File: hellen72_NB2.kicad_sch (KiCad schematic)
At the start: 186 parts, among them J1 USB_B_Mini, J11 Conn_01x01, J13 Conn_01x01, J14 Conn_01x01, J15 Conn_01x01, J16 Conn_01x01, J17 Conn_01x01, J19 Conn_01x01, J2 Conn_01x05_Male, J20 Conn_01x01, J21 Conn_01x01, J22 Conn_01x01, J24 Conn_01x01, J25 AudioJack3_SwitchTR, J27 Conn_01x06, J3 MiniFit, J4 Conn_02x12_Odd_Even, J5 USB_B, M1 Module-input-0.1, M10 Module-power12-0.2, M11 Module-power5-0.2, M12 Module-wbo-0.3, M13 Module-can-0.1, M2 Module-ign8-0.1, M3 Module-mcu-0.6, M4 Module-sd-0.1, M5 Module-output-0.3, M6 Module-dinput4-0.1, M7 Module-stlink-0.1, M8 Module-can-0.1, M9 Module-knock-0.1, P1 Pad, P10 Pad, P11 Pad, P12 Pad, P13 Pad, P15 Pad, P16 Pad, P17 Pad, P18 Pad, P19 Pad, P2 8-5353015-1, P20 Pad, P21 Pad, P23 Pad, P3 Pad, P4 Pad, P48 Pad, P49 Pad, P5 Pad, P50 Pad, P51 Pad, P52 Pad, P53 Pad, P56 Pad, P6 Pad, P7 Pad, P8 Pad, P9 Pad, Q1 AUIPS2041LTR, Q2 AUIPS2041LTR, U1 LIS2DW12TR, U2 MPX4_MAP, U3 MCP6002-xSN, U4 LPS25HB, U5 L6205PD

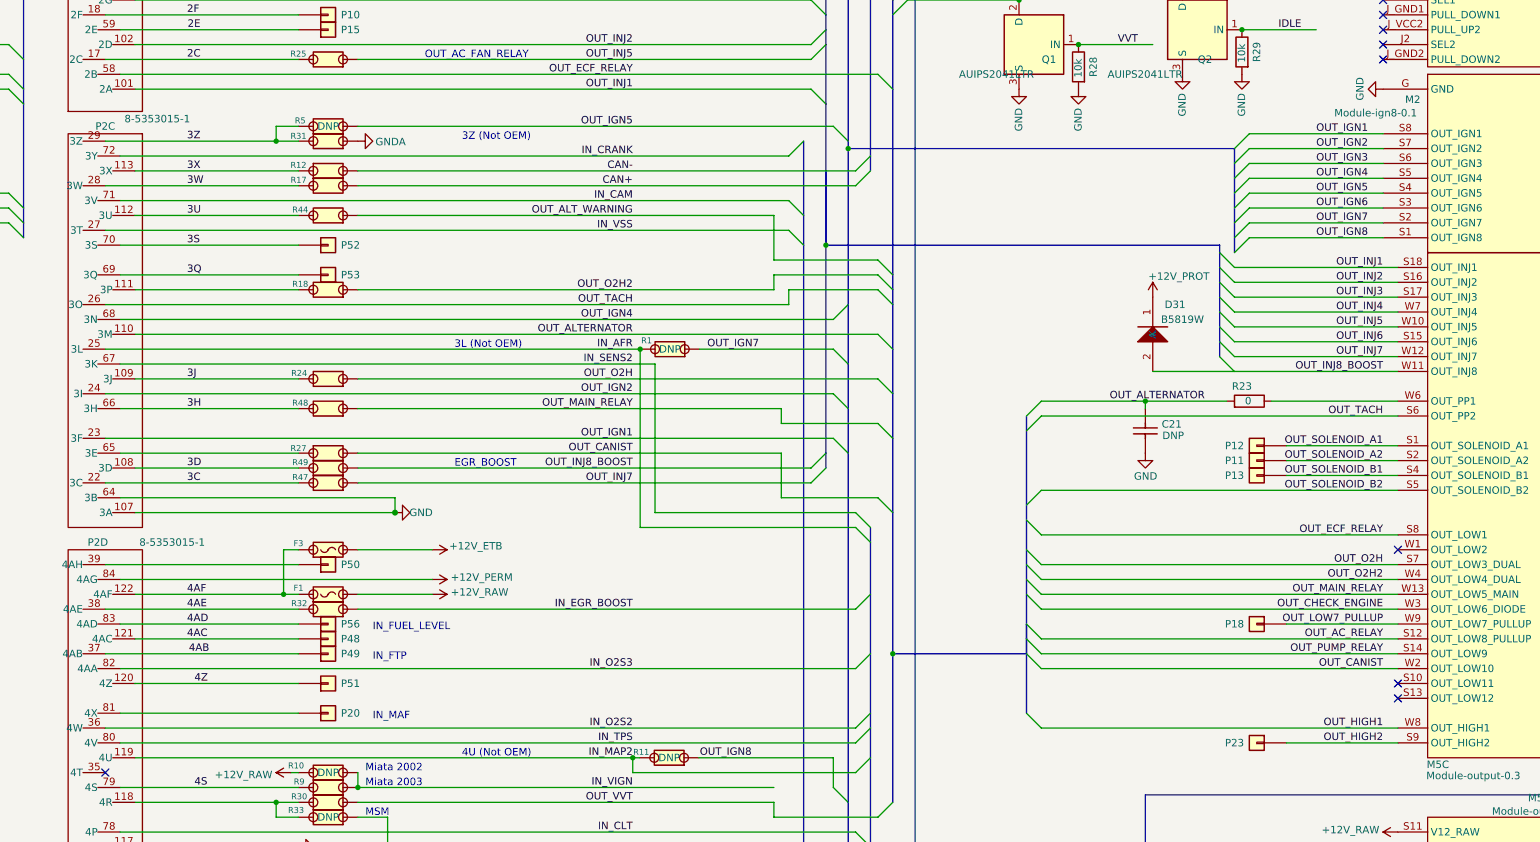
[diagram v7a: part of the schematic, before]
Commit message: https://github.com/rusefi/hellen-NB2-issues/issues/35
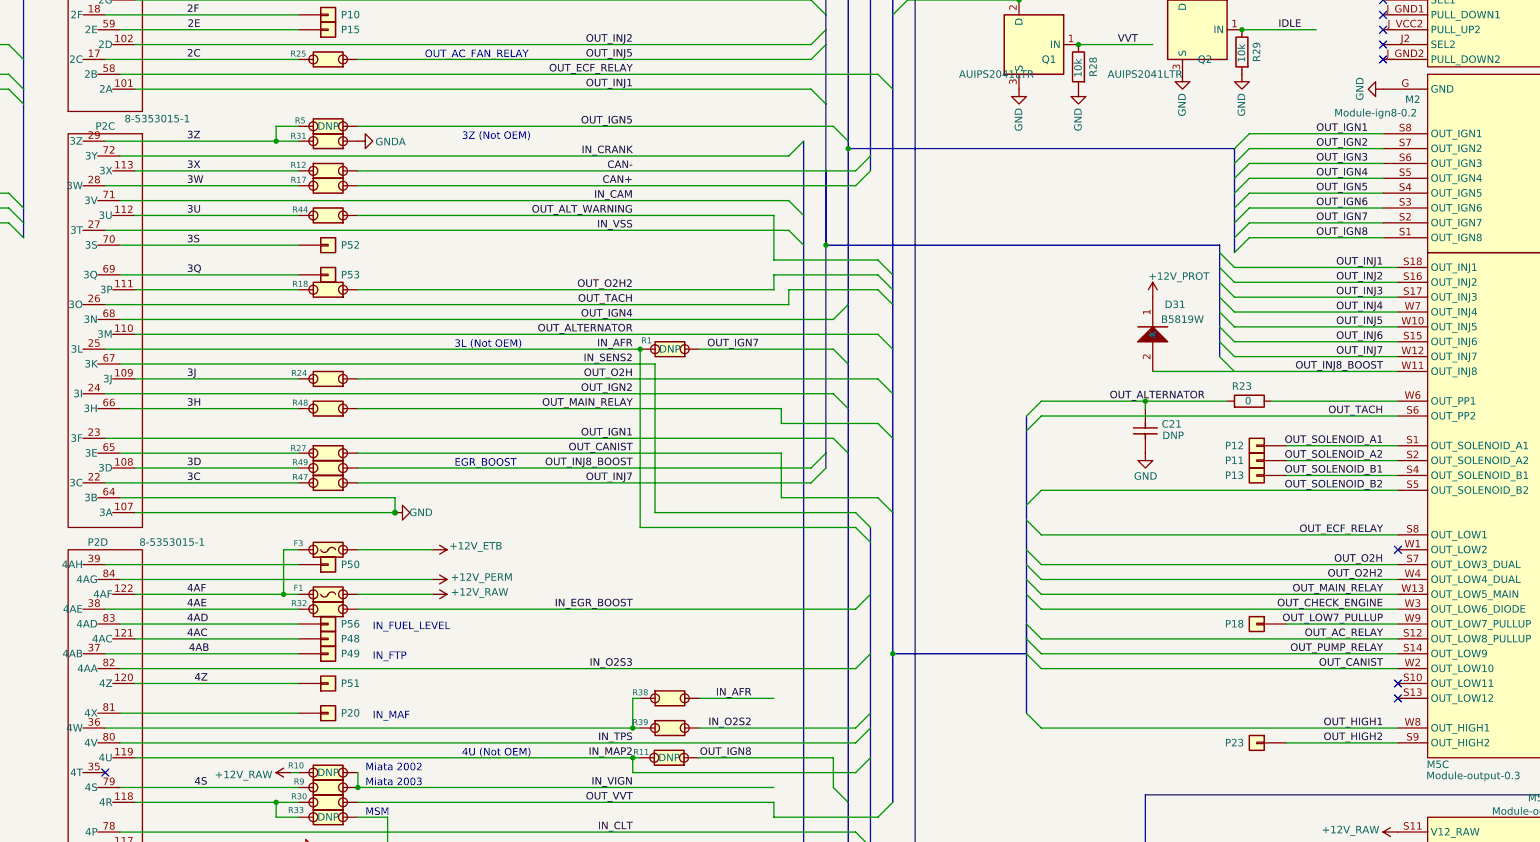
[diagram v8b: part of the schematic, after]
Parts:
- added R38, R39: Jumper-Pad-Pad, hellen-one-common:PAD-0805-PAD, symbol hellen-one-common:Jumper-Pad-Pad
- M2: value Module-ign8-0.1 -> Module-ign8-0.2; footprint hellen-one-ign8-0.1:ign8 -> hellen-one-ign8-0.2:ign8; symbol hellen-one-ign8-0.1:Module-ign8-0.1 -> hellen-one-ign8-0.2:Module-ign8-0.2
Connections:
- net IN_AFR: now also R38.2
- net IN_O2S2: now also R39.2; no longer P2.36 (4W)
- new net: P2.36 (4W), R38.1, R39.1
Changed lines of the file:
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@@
   (title_block
     (title "Hellen72 NB2")
-    (date "2022-03-28")
+    (date "2022-05-18")
     (rev "F")
     (company "rusEFI")
@@
   (junction (at 567.69 325.12) (diameter 1.016) (color 0 0 0 0)
   )
+  (junction (at 179.07 172.72) (diameter 0) (color 0 0 0 0)
+  )
   (junction (at 513.08 308.61) (diameter 1.016) (color 0 0 0 0)
   )
@@
     (stroke (width 0) (type solid) (color 0 0 0 0))
   )
+  (wire (pts (xy 179.07 172.72) (xy 180.34 172.72))
+    (stroke (width 0) (type solid) (color 0 0 0 0))
+  )
+  (wire (pts (xy 190.5 172.72) (xy 217.17 172.72))
+    (stroke (width 0) (type solid) (color 0 0 0 0))
+  )
   (wire (pts (xy 120.65 180.34) (xy 121.92 180.34))
     (stroke (width 0) (type default) (color 0 0 0 0))
@@
     (stroke (width 0) (type solid) (color 0 0 0 0))
   )
+  (wire (pts (xy 179.07 167.64) (xy 179.07 172.72))
+    (stroke (width 0) (type default) (color 0 0 0 0))
+  )
   (wire (pts (xy 88.9 123.19) (xy 213.36 123.19))
     (stroke (width 0) (type default) (color 0 0 0 0))
@@
     (stroke (width 0) (type solid) (color 0 0 0 0))
   )
-  (wire (pts (xy 88.9 172.72) (xy 217.17 172.72))
+  (wire (pts (xy 88.9 172.72) (xy 179.07 172.72))
     (stroke (width 0) (type solid) (color 0 0 0 0))
   )
@@
     (stroke (width 0) (type solid) (color 0 0 0 0))
   )
+  (wire (pts (xy 180.34 167.64) (xy 179.07 167.64))
+    (stroke (width 0) (type default) (color 0 0 0 0))
+  )
   (wire (pts (xy 203.2 33.02) (xy 203.2 35.56))
     (stroke (width 0) (type default) (color 0 0 0 0))
@@
     (stroke (width 0) (type solid) (color 0 0 0 0))
   )
+  (wire (pts (xy 190.5 167.64) (xy 203.2 167.64))
+    (stroke (width 0) (type default) (color 0 0 0 0))
+  )
   (bus (pts (xy 273.05 262.89) (xy 273.05 265.43))
     (stroke (width 0.3048) (type solid) (color 255 0 255 1))
@@
     (effects (font (size 1.27 1.27)) (justify right bottom))
   )
+  (label "IN_AFR" (at 199.39 167.64 180)
+    (effects (font (size 1.27 1.27)) (justify right bottom))
+  )
   (label "IN_SENS3" (at 179.07 300.99 180)
     (effects (font (size 1.27 1.27)) (justify right bottom))
@@
     (effects (font (size 1.27 1.27)) (justify right bottom))
   )
-  (label "IN_O2S2" (at 179.07 172.72 180)
+  (label "IN_O2S2" (at 199.39 172.72 180)
     (effects (font (size 1.27 1.27)) (justify right bottom))
   )
@@
     (pin "1")
   )
+  (symbol (lib_id "hellen-one-common:Jumper-Pad-Pad") (at 185.42 167.64 0) (mirror x) (unit 1)
+    (in_bom yes) (on_board yes)
+    (property "Reference" "R38" (id 0) (at 180.3639 166.6584 0)
+      (effects (font (size 1.016 1.016)))
+    )
+    (property "Value" "Jumper-Pad-Pad" (id 1) (at 185.42 165.862 0)
+      (effects (font (size 1.016 1.016)) hide)
+    )
+    (property "Footprint" "hellen-one-common:PAD-0805-PAD" (id 2) (at 185.42 163.83 0)
+      (effects (font (size 1.524 1.524)) hide)
+    )
+    (property "Datasheet" "" (id 3) (at 185.42 167.64 0)
+      (effects (font (size 1.524 1.524)) hide)
+    )
+    (property "LCSC" " C17477" (id 4) (at 185.42 163.83 0)
+      (effects (font (size 1.27 1.27)) hide)
+    )
+    (pin "1")
+    (pin "2")
+  )
   (symbol (lib_id "hellen-one-common:+12V_PERM") (at 144.78 147.32 270) (mirror x) (unit 1)
     (in_bom yes) (on_board yes)
@@
     (pin "9")
   )
+  (symbol (lib_id "hellen-one-common:Jumper-Pad-Pad") (at 185.42 172.72 0) (mirror x) (unit 1)
+    (in_bom yes) (on_board yes)
+    (property "Reference" "R39" (id 0) (at 180.3639 171.7384 0)
+      (effects (font (size 1.016 1.016)))
+    )
+    (property "Value" "Jumper-Pad-Pad" (id 1) (at 185.42 170.942 0)
+      (effects (font (size 1.016 1.016)) hide)
+    )
+    (property "Footprint" "hellen-one-common:PAD-0805-PAD" (id 2) (at 185.42 168.91 0)
+      (effects (font (size 1.524 1.524)) hide)
+    )
+    (property "Datasheet" "" (id 3) (at 185.42 172.72 0)
+      (effects (font (size 1.524 1.524)) hide)
+    )
+    (property "LCSC" " C17477" (id 4) (at 185.42 168.91 0)
+      (effects (font (size 1.27 1.27)) hide)
+    )
+    (pin "1")
+    (pin "2")
+  )
   (symbol (lib_id "hellen-one-common:Pad") (at 285.75 127 0) (mirror y) (unit 1)
     (in_bom yes) (on_board yes)
@@
     (pin "W8")
   )
-  (symbol (lib_id "hellen-one-ign8-0.1:Module-ign8-0.1") (at 347.98 60.96 0) (mirror y) (unit 1)
+  (symbol (lib_id "hellen-one-ign8-0.2:Module-ign8-0.2") (at 347.98 60.96 0) (mirror y) (unit 1)
     (in_bom yes) (on_board yes)
     (property "Reference" "M2" (id 0) (at 312.42 65.2738 0))
-    (property "Value" "Module-ign8-0.1" (id 1) (at 306.07 67.5725 0))
-    (property "Footprint" "hellen-one-ign8-0.1:ign8" (id 2) (at 347.98 60.96 0)
+    (property "Value" "Module-ign8-0.2" (id 1) (at 306.07 67.5725 0))
+    (property "Footprint" "hellen-one-ign8-0.2:ign8" (id 2) (at 347.98 60.96 0)
       (effects (font (size 1.27 1.27)) hide)
     )
@@
     )
     (path "/91b56abf-9ad5-4be8-a5c5-2398d74dccc7"
-      (reference "M2") (unit 1) (value "Module-ign8-0.1") (footprint "hellen-one-ign8-0.1:ign8")
+      (reference "M2") (unit 1) (value "Module-ign8-0.2") (footprint "hellen-one-ign8-0.2:ign8")
     )
     (path "/a6bf355d-1d5f-4e79-8e3f-45e3bddf3ceb"
@@
       (reference "R37") (unit 1) (value "Jumper-Pad-Pad") (footprint "hellen-one-common:PAD-0805-PAD")
     )
+    (path "/1362084f-c679-4679-89df-098bf460a1b1"
+      (reference "R38") (unit 1) (value "Jumper-Pad-Pad") (footprint "hellen-one-common:PAD-0805-PAD")
+    )
+    (path "/2d047ac0-e4c7-41d2-8948-269f409bfaf1"
+      (reference "R39") (unit 1) (value "Jumper-Pad-Pad") (footprint "hellen-one-common:PAD-0805-PAD")
+    )
     (path "/a33e8d5e-7e08-4789-b68e-c3ff24c44ffb"
